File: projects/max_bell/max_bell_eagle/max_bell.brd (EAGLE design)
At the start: 68.2 x 64.8 mm, 23 parts

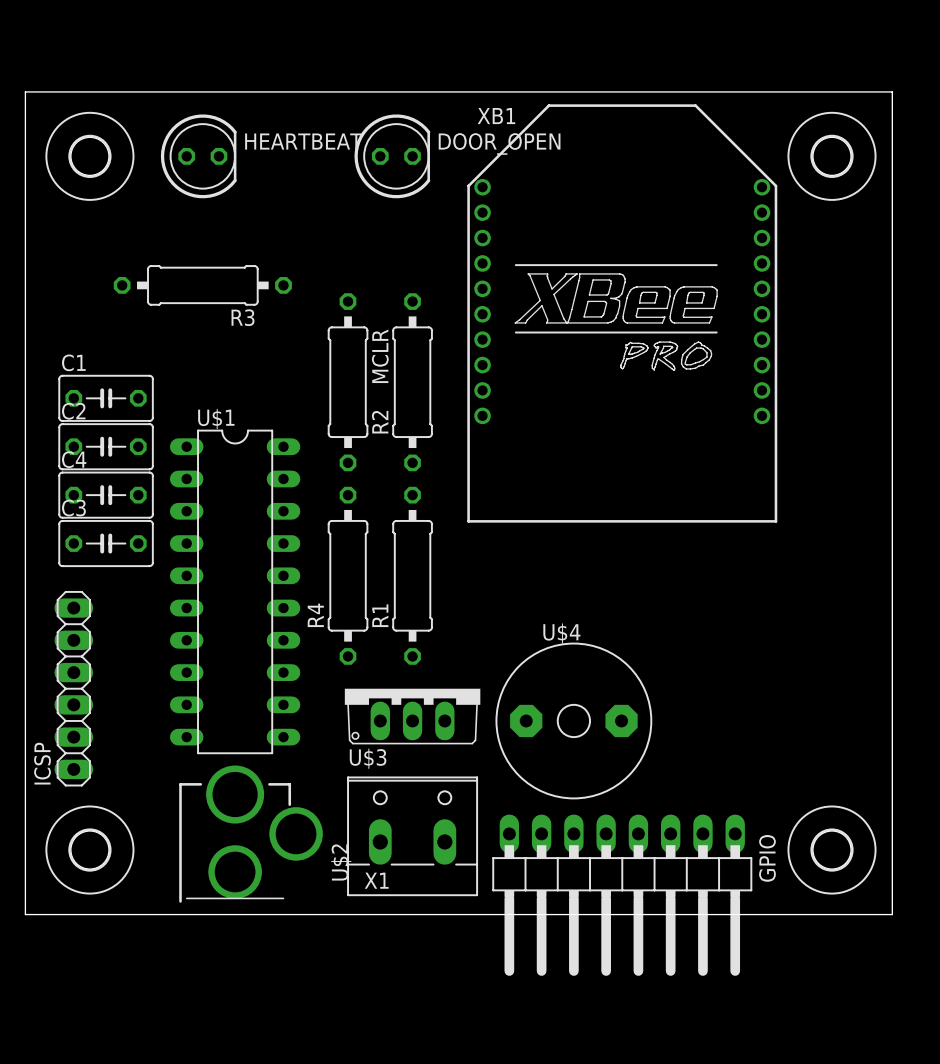
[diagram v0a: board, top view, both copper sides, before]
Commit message: update max_bell drawing, start mplab firmware
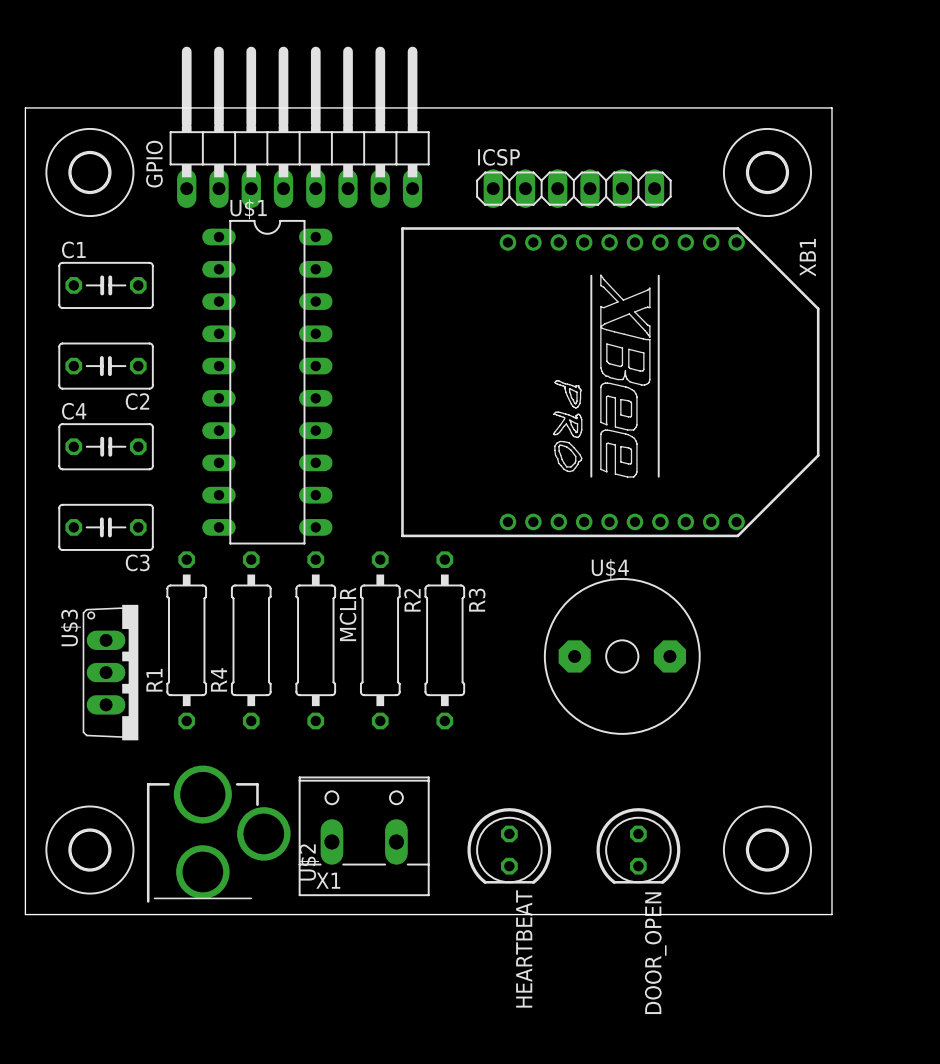
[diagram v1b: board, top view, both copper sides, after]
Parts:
- moved GPIO 63.7 mm to (21.6, 61.0), turned to 0 degrees
- moved HEARTBEAT 59.7 mm to (38.1, 5.08), turned to 270 degrees
- moved DOOR_OPEN 57.8 mm to (48.3, 5.08), turned to 270 degrees
- moved ICSP 55.7 mm to (43.2, 57.1), turned to 0 degrees
- moved R3 33.8 mm to (33.0, 21.6), turned to 270 degrees
- moved U$3 25.9 mm to (5.08, 19.1), turned to 270 degrees
- moved MCLR 20.5 mm to (22.9, 21.6)
- moved R2 20.5 mm to (27.9, 21.6), turned to 270 degrees
- moved R1 18.5 mm to (12.7, 21.6)
- moved U$1 16.7 mm to (19.1, 41.9)
- moved R4 9.16 mm to (17.8, 21.6)
- moved C1 8.89 mm to (6.35, 49.5)
- moved C2 6.35 mm to (6.35, 43.2), turned to 180 degrees
- moved U$4 6.35 mm to (47.0, 20.3)
- moved XB1 6.35 mm to (47.0, 41.9), turned to 270 degrees
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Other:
- board size 68.2 x 64.8 mm -> 63.5 x 63.5 mm

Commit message: updates to max_bell
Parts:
- removed GPIO: (no value), pinhead:1X08/90
- added JP1: (no value), pinhead:1X10
- added R5: 10K, rcl:0309/12
- added U$9: (no value), holes:3,0
- R2: value 1K -> 10K
- U$5: value (none) -> SWITCH_MOMENTARY; device holes:3,0 -> fritz:MOMENTARY_SWITCH
- moved U$5 61.9 mm to (61.0, 31.8), turned to 90 degrees
- moved U$8 60.0 mm to (64.8, 64.8)
- moved HEARTBEAT 54.6 mm to (61.0, 54.6), turned to 90 degrees
- moved U$7 53.7 mm to (64.8, 5.08)
- moved U$6 53.3 mm to (5.08, 5.08)
- moved DOOR_OPEN 41.4 mm to (61.0, 44.5), turned to 90 degrees
- moved ICSP 38.9 mm to (5.08, 49.5), turned to 90 degrees
- moved XB1 26.7 mm to (22.9, 53.3), turned to 0 degrees
- moved C1 24.7 mm to (11.4, 25.4), turned to 90 degrees
- moved C2 21.1 mm to (17.8, 25.4), turned to 90 degrees
- moved C4 20.9 mm to (11.4, 16.5), turned to 90 degrees
- moved U$1 20.8 mm to (35.6, 29.2), turned to 0 degrees
- moved C3 18.1 mm to (17.8, 16.5), turned to 270 degrees
- moved R2 16.6 mm to (44.5, 20.3), turned to 0 degrees
- moved U$4 14.5 mm to (61.0, 16.5), turned to 270 degrees
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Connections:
- net GND: now also JP1.1, U$5.4; no longer U$4.2
- net GPIO_0: now also JP1.3; no longer GPIO.1
- net GPIO_1: now also JP1.4; no longer GPIO.2
- net GPIO_2: now also JP1.5, R5.1, U$5.1; no longer GPIO.3
- net GPIO_3: now also JP1.6; no longer GPIO.4
- net GPIO_4: now also JP1.7; no longer GPIO.5
- net GPIO_5: now also JP1.8; no longer GPIO.6
- net GPIO_6: now also JP1.9; no longer GPIO.7
- net GPIO_7: now also JP1.10; no longer GPIO.8
- net ICSPCLK: now also U$1.18
- net ICSPDAT: now also U$1.19
- net VDD: now also JP1.2, R5.2, U$4.2
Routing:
- net GND: track 0.00 -> 208.4 mm, vias 0 -> 10
- net VDD: track 0.00 -> 151.0 mm
- net GPIO_0: track 0.00 -> 88.5 mm
- net GPIO_1: track 0.00 -> 82.1 mm
- net TERMINAL_BLOCK: track 0.00 -> 81.0 mm
- net TX: track 0.00 -> 78.2 mm
- net GPIO_2: track 0.00 -> 68.5 mm
- net BUZZER: track 0.00 -> 51.6 mm
- net RX: track 0.00 -> 47.6 mm, vias 0 -> 2
- net GPIO_5: track 0.00 -> 45.5 mm
- net GPIO_4: track 0.00 -> 44.0 mm
- net N$4: track 0.00 -> 39.8 mm
- net ICSPCLK: track 0.00 -> 36.3 mm
- net ICSPDAT: track 0.00 -> 35.5 mm
- net N$5: track 0.00 -> 34.7 mm
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- added copper zone on layer 1, net GND
- added copper zone on layer 16, net GND
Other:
- board size 63.5 x 63.5 mm -> 70 x 70 mm
- board text added: "+V"
- board text added: "0"
- board text added: "02.2014"
- board text added: "1"
- board text added: "7"
- board text added: "DOOR!"
- board text added: "FRITZ"
- board text added: "G"
- board text added: "GO TO SLEEP"
- board text added: "GPIO"
- board text added: "HEARTBEAT"
- board text added: "ISCP"
- board text added: "RESET"
- board text added: "REV"

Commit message: max_bell done
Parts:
- moved U$6 59.7 mm to (5.08, 64.8)
- moved U$7 59.7 mm to (64.8, 64.8)
- moved U$8 59.7 mm to (64.8, 5.08)
- moved U$9 59.7 mm to (5.08, 5.08)
- moved C1 2.54 mm to (11.4, 27.9)
- moved C2 2.54 mm to (17.8, 27.9)
- moved XB1 2.54 mm to (25.4, 53.3)
- moved HEARTBEAT 1.80 mm to (62.2, 53.3)
- moved ICSP 1.27 mm to (5.08, 48.3)
- moved C3 1.27 mm to (17.8, 17.8), turned to 90 degrees
- moved C4 1.27 mm to (11.4, 17.8)
- moved U$1 1.27 mm to (35.6, 27.9)
- moved DOOR_OPEN 1.27 mm to (62.2, 44.5)
- moved U$4 1.27 mm to (62.2, 16.5), turned to 90 degrees
- moved U$5 1.27 mm to (62.2, 31.8)
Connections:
- new net BUTTON: R5.1, U$1.17, U$5.1
- net GPIO_2: no longer R5.1, U$5.1
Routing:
- net BUTTON: track 0.00 -> 51.7 mm
- net GND: track 208.4 -> 161.9 mm, vias 10 -> 8
- net GPIO_2: track 68.5 -> 29.3 mm
- net TERMINAL_BLOCK: track 81.0 -> 58.4 mm
- net GPIO_1: track 82.1 -> 59.9 mm
- net GPIO_0: track 88.5 -> 66.5 mm
- net TX: track 78.2 -> 58.0 mm
- net GPIO_4: track 44.0 -> 30.8 mm, vias 0 -> 1
- net ICSPCLK: track 36.3 -> 46.2 mm
- net RX: track 47.6 -> 57.1 mm, vias 2 -> 1
- net VDD: track 151.0 -> 159.5 mm
- net ICSPDAT: track 35.5 -> 31.2 mm
- net GPIO_7: track 33.5 -> 29.3 mm
- net GPIO_3: track 27.0 -> 22.7 mm
- net BUZZER: track 51.6 -> 55.2 mm
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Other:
- board text added: "+"
- board text added: "2"
- board text added: "3"
- board text added: "4"
- board text added: "5"
- board text added: "6"
- board text added: "ONLY ON WAKING DO WE KNOW IT WAS A DREAM"
- board text added: "unitstep"
- board text removed: "GPIO"
- board text removed: "ISCP"
